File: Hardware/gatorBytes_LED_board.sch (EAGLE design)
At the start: 44 parts

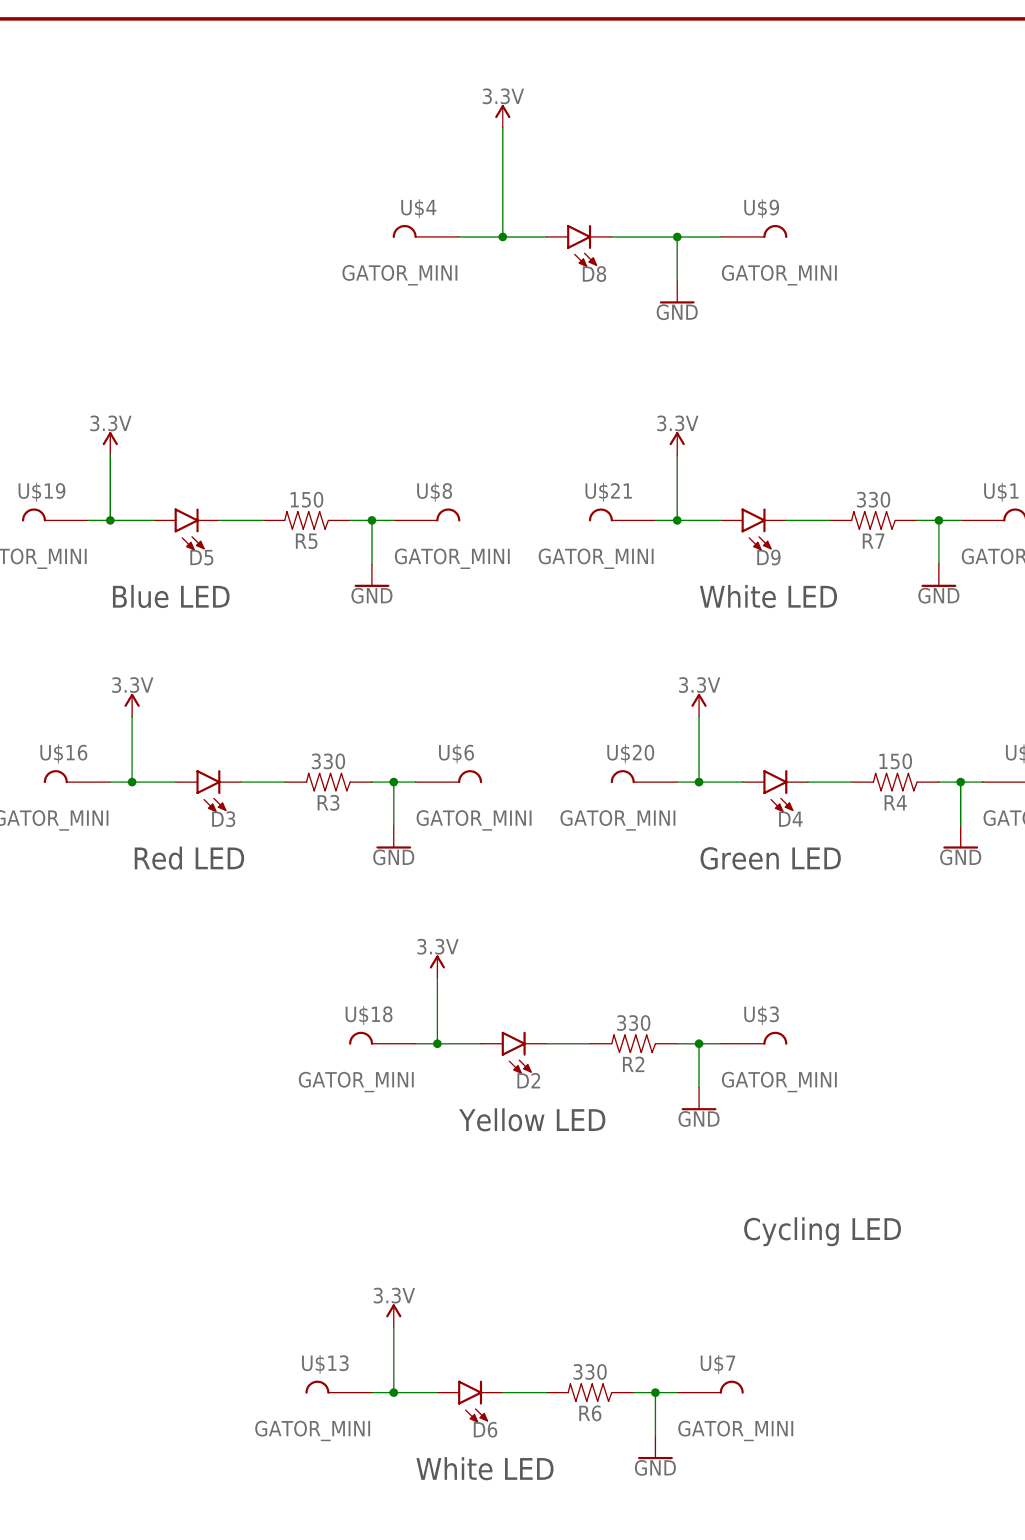
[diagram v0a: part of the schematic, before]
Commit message: removing pth
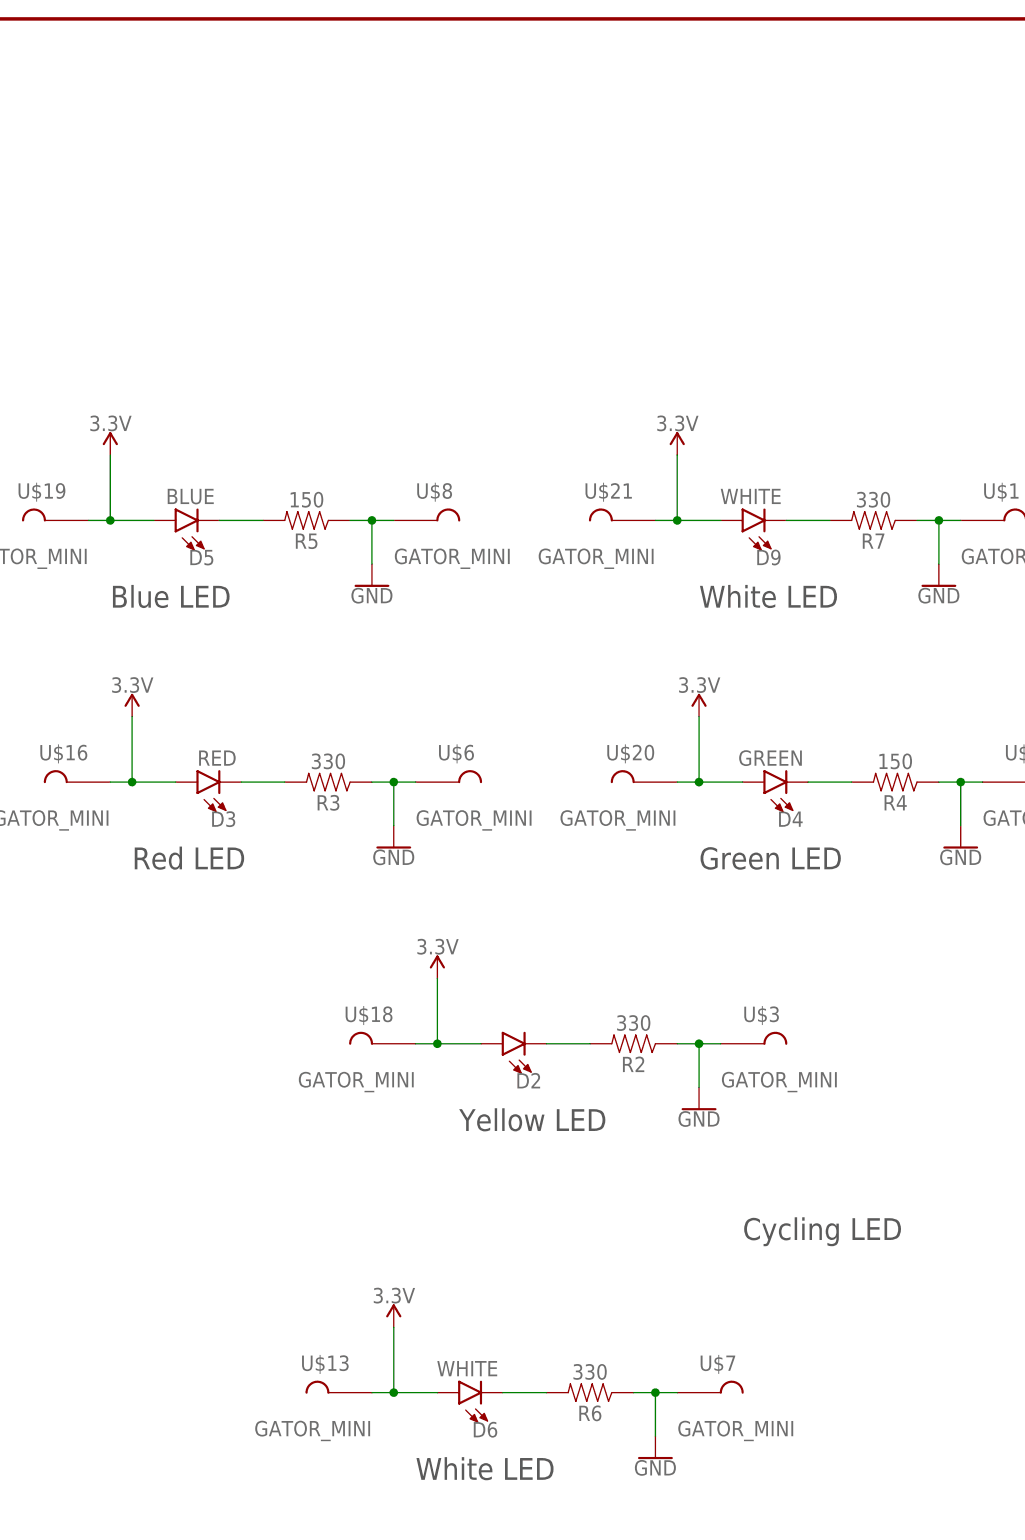
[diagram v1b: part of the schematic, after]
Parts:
- removed D8: (no value), SparkFun-LED:LED5MM-KIT
- removed U$4, U$9: GATOR_MINI, TAB:GATOR_MINI
- D2: device SparkFun-LED:LED5MM -> SparkFun-LED:LED-YELLOW_HIDDENSILK
- D3: value (none) -> RED; device SparkFun-LED:LED5MM -> SparkFun-LED:LED-RED1206
- D4: value (none) -> GREEN; device SparkFun-LED:LED5MM -> SparkFun-LED:LED-GREEN1206
- D5: value (none) -> BLUE; device SparkFun-LED:LED5MM -> SparkFun-LED:LED-BLUE1206
- D6, D9: value (none) -> WHITE; device SparkFun-LED:LED5MM -> SparkFun-LED:LED-WHITE1206
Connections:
- net 3.3V: no longer D8.A, U$4.P$1
- net GND: no longer D8.C, U$9.P$1
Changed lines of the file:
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@@
 <?xml version="1.0" encoding="utf-8"?>
 <!DOCTYPE eagle SYSTEM "eagle.dtd">
-<eagle version="8.7.0">
+<eagle version="9.1.0">
 <drawing>
 <settings>
@@
 <parts>
 <part name="FRAME1" library="SparkFun-Aesthetics" deviceset="FRAME-LETTER" device=""/>
-<part name="D2" library="SparkFun-LED" deviceset="LED" device="5MM"/>
+<part name="D2" library="SparkFun-LED" deviceset="LED-YELLOW" device="_HIDDENSILK"/>
 <part name="R2" library="SparkFun-Resistors" deviceset="330OHM" device="-0603-1/10W-1%" value="330"/>
 <part name="SUPPLY2" library="SparkFun-PowerSymbols" deviceset="3.3V" device=""/>
 <part name="GND2" library="SparkFun-PowerSymbols" deviceset="GND" device=""/>
-<part name="D3" library="SparkFun-LED" deviceset="LED" device="5MM"/>
+<part name="D3" library="SparkFun-LED" deviceset="LED-RED" device="1206" value="RED"/>
 <part name="R3" library="SparkFun-Resistors" deviceset="330OHM" device="-0603-1/10W-1%" value="330"/>
 <part name="SUPPLY3" library="SparkFun-PowerSymbols" deviceset="3.3V" device=""/>
 <part name="GND3" library="SparkFun-PowerSymbols" deviceset="GND" device=""/>
-<part name="D4" library="SparkFun-LED" deviceset="LED" device="5MM"/>
+<part name="D4" library="SparkFun-LED" deviceset="LED-GREEN" device="1206" value="GREEN"/>
 <part name="R4" library="SparkFun-Resistors" deviceset="150OHM" device="-0603-1/10W-1%" value="150"/>
 <part name="SUPPLY4" library="SparkFun-PowerSymbols" deviceset="3.3V" device=""/>
 <part name="GND4" library="SparkFun-PowerSymbols" deviceset="GND" device=""/>
-<part name="D5" library="SparkFun-LED" deviceset="LED" device="5MM"/>
+<part name="D5" library="SparkFun-LED" deviceset="LED-BLUE" device="1206" value="BLUE"/>
 <part name="R5" library="SparkFun-Resistors" deviceset="150OHM" device="-0603-1/10W-1%" value="150"/>
 <part name="SUPPLY5" library="SparkFun-PowerSymbols" deviceset="3.3V" device=""/>
 <part name="GND5" library="SparkFun-PowerSymbols" deviceset="GND" device=""/>
-<part name="D6" library="SparkFun-LED" deviceset="LED" device="5MM"/>
+<part name="D6" library="SparkFun-LED" deviceset="LED-WHITE" device="1206" value="WHITE"/>
 <part name="R6" library="SparkFun-Resistors" deviceset="330OHM" device="-0603-1/10W-1%" value="330"/>
 <part name="SUPPLY6" library="SparkFun-PowerSymbols" deviceset="3.3V" device=""/>
 <part name="GND6" library="SparkFun-PowerSymbols" deviceset="GND" device=""/>
-<part name="D8" library="SparkFun-LED" deviceset="LED" device="5MM-KIT"/>
-<part name="D9" library="SparkFun-LED" deviceset="LED" device="5MM"/>
+<part name="D9" library="SparkFun-LED" deviceset="LED-WHITE" device="1206" value="WHITE"/>
 <part name="R7" library="SparkFun-Resistors" deviceset="330OHM" device="-0603-1/10W-1%" value="330"/>
 <part name="SUPPLY7" library="SparkFun-PowerSymbols" deviceset="3.3V" device=""/>
 <part name="GND7" library="SparkFun-PowerSymbols" deviceset="GND" device=""/>
-<part name="SUPPLY8" library="SparkFun-PowerSymbols" deviceset="3.3V" device=""/>
-<part name="GND8" library="SparkFun-PowerSymbols" deviceset="GND" device=""/>
 <part name="U$1" library="TAB" deviceset="GATOR_MINI" device=""/>
 <part name="U$2" library="TAB" deviceset="GATOR_MINI" device=""/>
 <part name="U$3" library="TAB" deviceset="GATOR_MINI" device=""/>
-<part name="U$4" library="TAB" deviceset="GATOR_MINI" device=""/>
 <part name="U$6" library="TAB" deviceset="GATOR_MINI" device=""/>
 <part name="U$7" library="TAB" deviceset="GATOR_MINI" device=""/>
 <part name="U$8" library="TAB" deviceset="GATOR_MINI" device=""/>
-<part name="U$9" library="TAB" deviceset="GATOR_MINI" device=""/>
 <part name="U$13" library="TAB" deviceset="GATOR_MINI" device=""/>
 <part name="U$16" library="TAB" deviceset="GATOR_MINI" device=""/>
@@
 <instance part="SUPPLY6" gate="G$1" x="66.04" y="33.02"/>
 <instance part="GND6" gate="1" x="96.52" y="17.78"/>
-<instance part="D8" gate="G$1" x="86.36" y="160.02" rot="R90"/>
 <instance part="D9" gate="G$1" x="106.68" y="127" rot="R90"/>
 <instance part="R7" gate="G$1" x="121.92" y="127" rot="R180"/>
 <instance part="SUPPLY7" gate="G$1" x="99.06" y="134.62"/>
 <instance part="GND7" gate="1" x="129.54" y="119.38"/>
-<instance part="SUPPLY8" gate="G$1" x="78.74" y="172.72"/>
-<instance part="GND8" gate="1" x="99.06" y="152.4"/>
 <instance part="U$1" gate="G$1" x="134.62" y="127"/>
 <instance part="U$2" gate="G$1" x="137.16" y="96.52"/>
 <instance part="U$3" gate="G$1" x="106.68" y="66.04"/>
-<instance part="U$4" gate="G$1" x="71.12" y="160.02" rot="MR0"/>
 <instance part="U$6" gate="G$1" x="71.12" y="96.52"/>
 <instance part="U$7" gate="G$1" x="101.6" y="25.4"/>
 <instance part="U$8" gate="G$1" x="68.58" y="127"/>
-<instance part="U$9" gate="G$1" x="106.68" y="160.02"/>
 <instance part="U$13" gate="G$1" x="60.96" y="25.4" rot="MR0"/>
 <instance part="U$16" gate="G$1" x="30.48" y="96.52" rot="MR0"/>
@@
 </segment>
 <segment>
-<pinref part="D8" gate="G$1" pin="A"/>
-<wire x1="73.66" y1="160.02" x2="78.74" y2="160.02" width="0.1524" layer="91"/>
-<pinref part="SUPPLY8" gate="G$1" pin="3.3V"/>
-<wire x1="78.74" y1="160.02" x2="83.82" y2="160.02" width="0.1524" layer="91"/>
-<wire x1="78.74" y1="172.72" x2="78.74" y2="160.02" width="0.1524" layer="91"/>
-<junction x="78.74" y="160.02"/>
-<pinref part="U$4" gate="G$1" pin="P$1"/>
-</segment>
-<segment>
 <pinref part="U$34" gate="G$1" pin="P$1"/>
 <wire x1="198.12" y1="68.58" x2="198.12" y2="78.74" width="0.1524" layer="91"/>
@@
 </segment>
 <segment>
-<pinref part="D8" gate="G$1" pin="C"/>
-<wire x1="91.44" y1="160.02" x2="99.06" y2="160.02" width="0.1524" layer="91"/>
-<pinref part="GND8" gate="1" pin="GND"/>
-<wire x1="99.06" y1="160.02" x2="104.14" y2="160.02" width="0.1524" layer="91"/>
-<wire x1="99.06" y1="154.94" x2="99.06" y2="160.02" width="0.1524" layer="91"/>
-<junction x="99.06" y="160.02"/>
-<pinref part="U$9" gate="G$1" pin="P$1"/>
-</segment>
-<segment>

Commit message: post checklist changes
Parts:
- D2: value (none) -> RED; device SparkFun-LED:LED-YELLOW_HIDDENSILK -> SparkFun-LED:LED-RED1206
- D3: value RED -> WHITE; device SparkFun-LED:LED-RED1206 -> SparkFun-LED:LED-WHITE1206
- D5: value BLUE -> Yellow; device SparkFun-LED:LED-BLUE1206 -> SparkFun-LED:LED-YELLOWLILYPAD
- D6: value WHITE -> GREEN; device SparkFun-LED:LED-WHITE1206 -> SparkFun-LED:LED-GREEN1206
- U$1, U$10, U$11, U$13, U$16, U$18, U$19, U$2, U$20, U$21, U$28, U$3, U$30, U$32, U$33, U$34, U$38, U$6, U$7, U$8: value GATOR_MINI -> TAB_GATOR_MINI; device TAB:GATOR_MINI -> SparkFun-Connectors:TAB_GATOR_MINI
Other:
- note added: "LED's"
- note added: "Power"
- note added: "v10"
- note removed: "Cycling LED"
- note removed: "Power Board"
- note removed: "V01"
- moved on the sheet: D2, D3, D4, D5, D6, D9, R2, R3, R4, R5, R6, R7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

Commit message: post checklist changes
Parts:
- added LOGO8: REVISION, SparkFun-Aesthetics:REVISION
- D4: value GREEN -> BLUE; device SparkFun-LED:LED-GREEN1206 -> SparkFun-LED:LED-BLUE1206
- R5: value 150 -> 330; device SparkFun-Resistors:150OHM-0603-1/10W-1% -> SparkFun-Resistors:330OHM-0603-1/10W-1%
- R6: value 330 -> 150; device SparkFun-Resistors:330OHM-0603-1/10W-1% -> SparkFun-Resistors:150OHM-0603-1/10W-1%
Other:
- note added: "A. England"
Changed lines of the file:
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@@
 <part name="SUPPLY3" library="SparkFun-PowerSymbols" deviceset="3.3V" device=""/>
 <part name="GND3" library="SparkFun-PowerSymbols" deviceset="GND" device=""/>
-<part name="D4" library="SparkFun-LED" deviceset="LED-GREEN" device="1206" value="GREEN"/>
+<part name="D4" library="SparkFun-LED" deviceset="LED-BLUE" device="1206" value="BLUE"/>
 <part name="R4" library="SparkFun-Resistors" deviceset="150OHM" device="-0603-1/10W-1%" value="150"/>
 <part name="SUPPLY4" library="SparkFun-PowerSymbols" deviceset="3.3V" device=""/>
 <part name="GND4" library="SparkFun-PowerSymbols" deviceset="GND" device=""/>
 <part name="D5" library="SparkFun-LED" deviceset="LED-YELLOW" device="LILYPAD" value="Yellow"/>
-<part name="R5" library="SparkFun-Resistors" deviceset="150OHM" device="-0603-1/10W-1%" value="150"/>
+<part name="R5" library="SparkFun-Resistors" deviceset="330OHM" device="-0603-1/10W-1%" value="330"/>
 <part name="SUPPLY5" library="SparkFun-PowerSymbols" deviceset="3.3V" device=""/>
 <part name="GND5" library="SparkFun-PowerSymbols" deviceset="GND" device=""/>
 <part name="D6" library="SparkFun-LED" deviceset="LED-GREEN" device="1206" value="GREEN"/>
-<part name="R6" library="SparkFun-Resistors" deviceset="330OHM" device="-0603-1/10W-1%" value="330"/>
+<part name="R6" library="SparkFun-Resistors" deviceset="150OHM" device="-0603-1/10W-1%" value="150"/>
 <part name="SUPPLY6" library="SparkFun-PowerSymbols" deviceset="3.3V" device=""/>
 <part name="GND6" library="SparkFun-PowerSymbols" deviceset="GND" device=""/>
@@
 <part name="U$32" library="SparkFun-Connectors" deviceset="TAB_GATOR_MINI" device=""/>
 <part name="U$38" library="SparkFun-Connectors" deviceset="TAB_GATOR_MINI" device=""/>
+<part name="LOGO8" library="SparkFun-Aesthetics" deviceset="REVISION" device=""/>
 </parts>
 <sheets>
 <sheet>
 <plain>
-<text x="66.04" y="63.5" size="2.54" layer="97" font="vector" ratio="15">Red LED</text>
-<text x="63.5" y="38.1" size="2.54" layer="97" font="vector" ratio="15">Yellow LED</text>
-<text x="66.04" y="88.9" size="2.54" layer="97" font="vector" ratio="15">Blue LED</text>
-<text x="66.04" y="114.3" size="2.54" layer="97" font="vector" ratio="15">Green LED</text>
-<text x="63.5" y="12.7" size="2.54" layer="97" font="vector" ratio="15">White LED</text>
+<text x="63.5" y="38.1" size="2.54" layer="97" font="vector" ratio="15">Red LED</text>
+<text x="66.04" y="88.9" size="2.54" layer="97" font="vector" ratio="15">Yellow LED</text>
+<text x="66.04" y="114.3" size="2.54" layer="97" font="vector" ratio="15">Blue LED</text>
+<text x="63.5" y="12.7" size="2.54" layer="97" font="vector" ratio="15">Green LED</text>
+<text x="66.04" y="63.5" size="2.54" layer="97" font="vector" ratio="15">White LED</text>
 <text x="66.04" y="137.16" size="2.54" layer="97" font="vector" ratio="15">White LED</text>
 <text x="166.116" y="11.43" size="2.032" layer="94" font="vector">M. West</text>
@@
 <text x="66.04" y="165.1" size="3.81" layer="97" font="vector">LED's</text>
 <text x="190.5" y="134.62" size="5.08" layer="97" font="vector">Power</text>
+<text x="168.656" y="7.112" size="2.032" layer="94" font="vector">A. England</text>
 </plain>
 <instances>
@@
 <instance part="U$32" gate="G$1" x="182.88" y="111.76" rot="MR0"/>
 <instance part="U$38" gate="G$1" x="210.82" y="127"/>
+<instance part="LOGO8" gate="G$1" x="148.59" y="7.112"/>
 </instances>
 <busses>
